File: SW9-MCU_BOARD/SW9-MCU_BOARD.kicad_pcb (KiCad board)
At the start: 4 copper layers, 38.1 x 37.5 mm, 18 parts, among them IC1 STM32L051C6T6, J1 Conn_ARM_JTAG_SWD_10, SW2 SW_Push, SW3 SW_SPDT, Y1 ABS25-32.768KHZ-6-T, Y2 8MHz

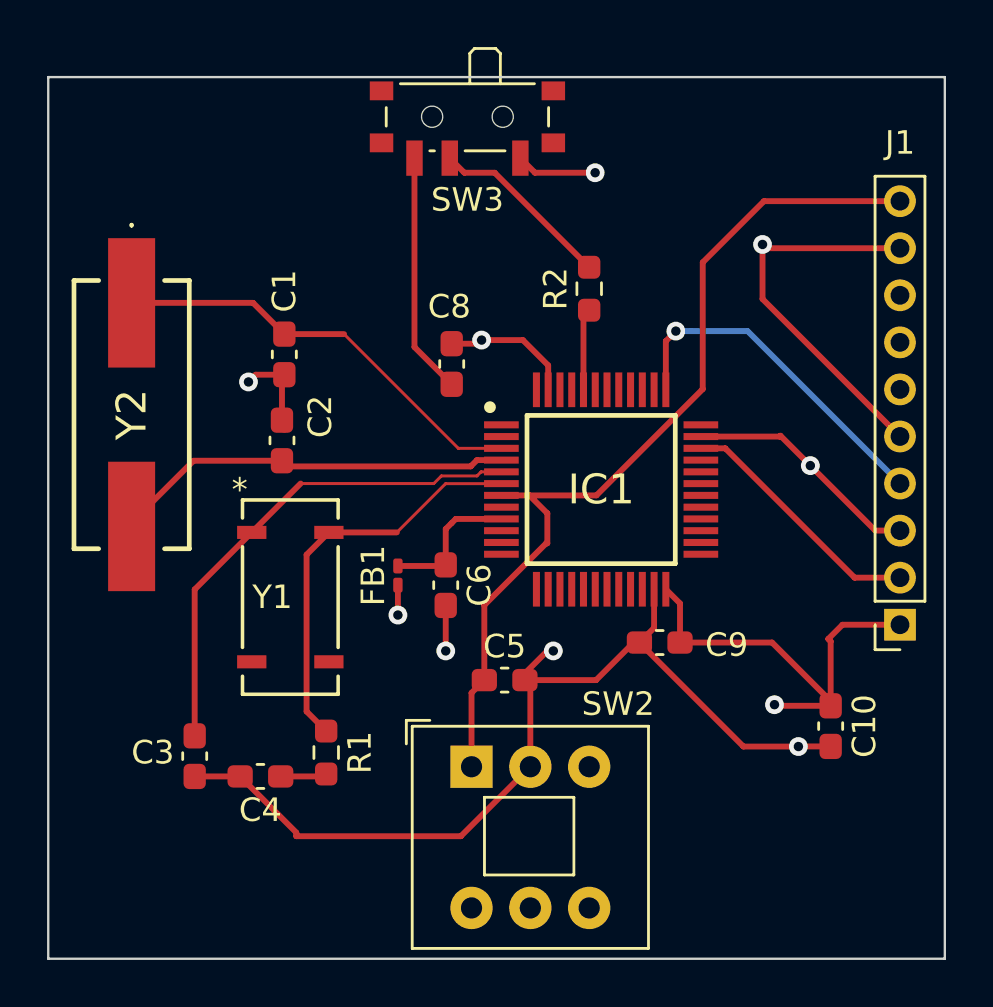
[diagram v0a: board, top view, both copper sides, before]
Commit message: change earth to gnd
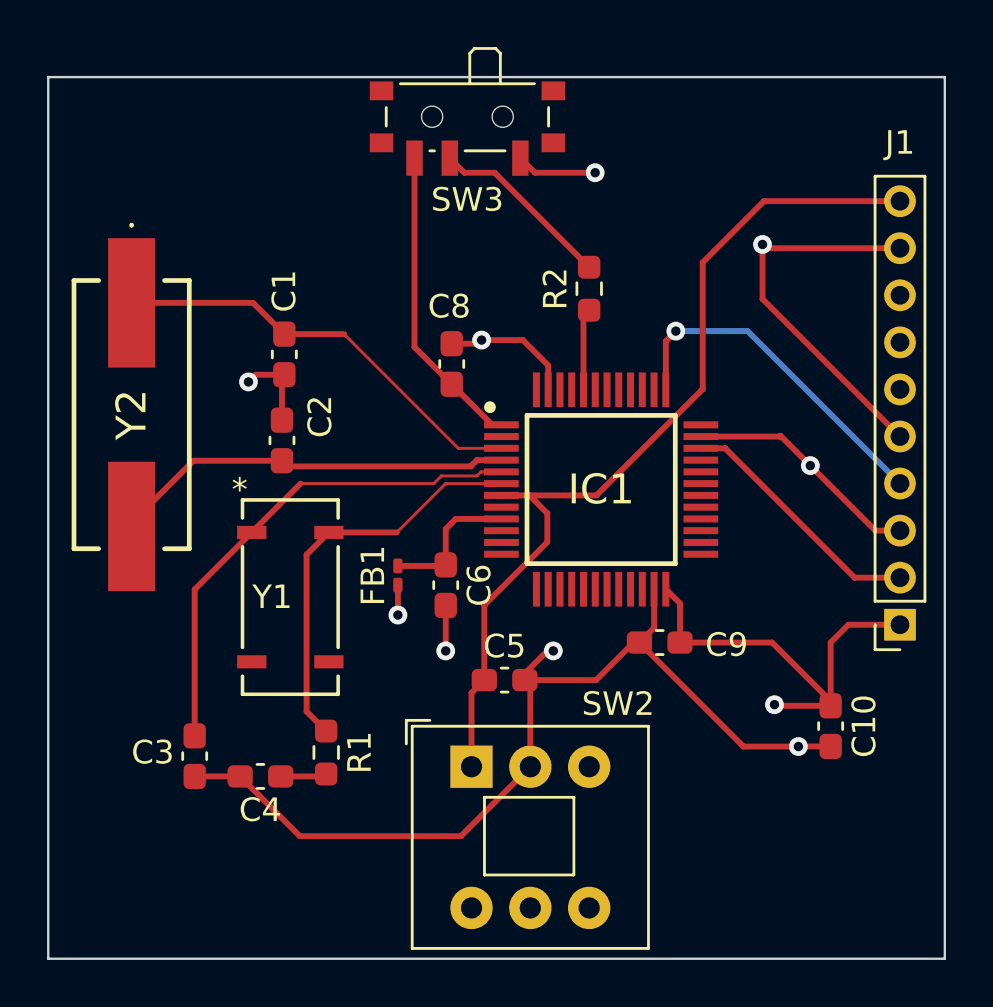
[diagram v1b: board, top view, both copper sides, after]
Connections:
- net Earth renamed GND
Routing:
- net VDD: track 30.3 -> 32.9 mm
